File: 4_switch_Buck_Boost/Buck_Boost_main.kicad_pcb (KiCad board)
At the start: 4 copper layers, 98 parts, among them J1 Conn_02x02_Counter_Clockwise, J2 Screw_Terminal_2x5.08, J3 Screw_Terminal_2x2.54, J4 Screw_Terminal_2x5.08, M1 Fan, Q1 CSD18532Q5B, Q101 2N7002K, Q103 BSS83P, Q2 CSD18532Q5B, Q3 CSD18532Q5B, Q4 CSD18532Q5B, Q6 AO3400A, U1 LT8390EUFD_PBF

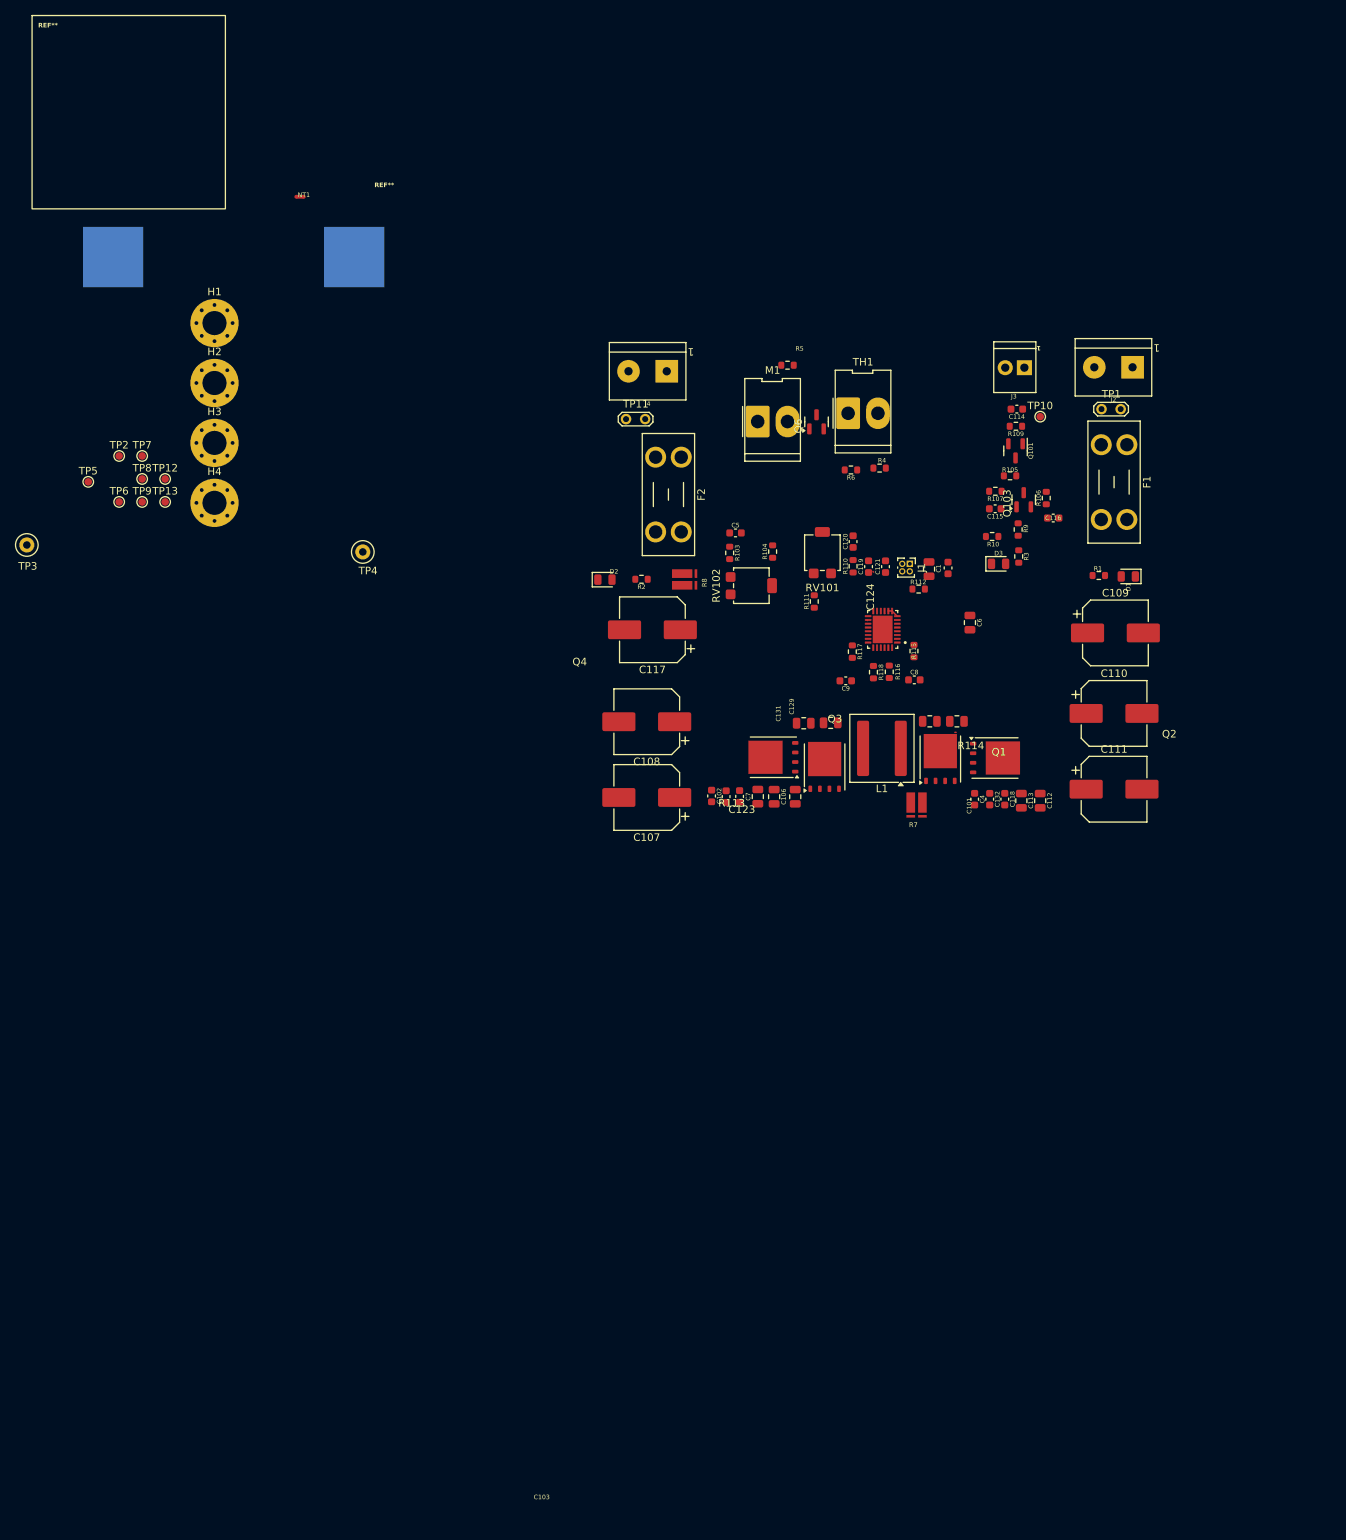
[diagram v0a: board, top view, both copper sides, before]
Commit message: improved Passive Components, Controller and Auxiliary Circuits
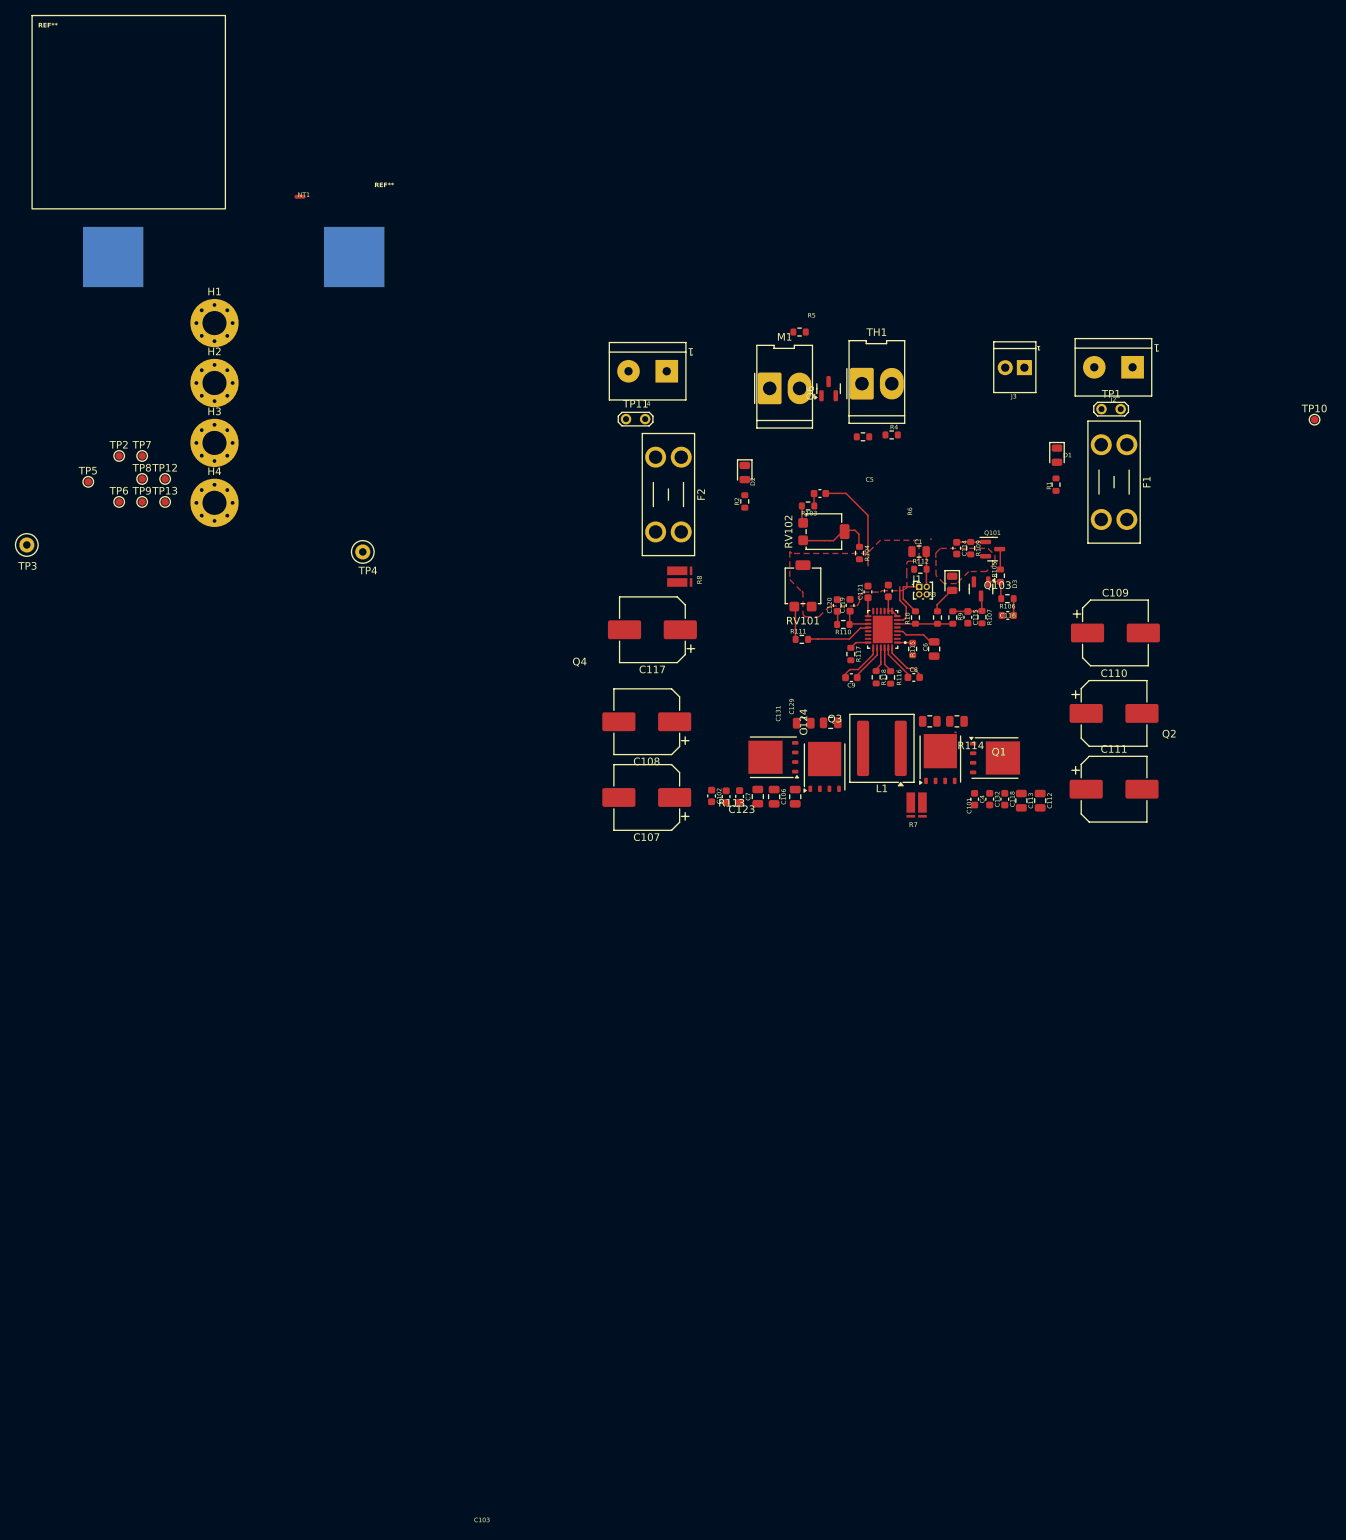
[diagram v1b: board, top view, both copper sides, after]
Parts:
- moved TP10 36.4 mm to (200.7, 73.0)
- moved D2 23.4 mm to (125.1, 80.0), turned to -90 degrees
- moved C114 20.1 mm to (153.2, 90.0), turned to -90 degrees
- moved D1 18.7 mm to (166.5, 77.7), turned to -90 degrees
- moved R109 17.3 mm to (155.1, 90.0), turned to -90 degrees
- moved R2 17.2 mm to (125.1, 83.8), turned to 90 degrees
- moved R107 16.8 mm to (156.6, 99.2), turned to -90 degrees
- moved C115 14.8 mm to (154.7, 99.2), turned to -90 degrees
- moved R10 14.8 mm to (147.8, 99.2), turned to 90 degrees
- moved R9 14.5 mm to (152.7, 99.2)
- moved R106 14.3 mm to (159.9, 96.7), turned to 180 degrees
- moved C116 14.3 mm to (160.0, 99.0), turned to 180 degrees
- moved R3 13.5 mm to (150.7, 99.2), turned to 90 degrees
- moved Q101 13.4 mm to (158.0, 90.2), turned to 0 degrees
- moved R1 13.3 mm to (166.4, 81.6), turned to 90 degrees
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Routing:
- net SYNC/SPRD: vias 0 -> 1
- net /INTVCC: vias 0 -> 1
- added copper zone on F.Cu, net GND
- added copper zone on F.Cu, net GNDA
- removed copper zone on In1.Cu, net GND

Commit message: Starting point for PCB Template Transformation
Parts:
- removed M1: Fan, Connector_Molex:Molex_KK-396_5273-02A_1x02_P3.96mm_Vertical
- removed Q6: AO3400A, Package_TO_SOT_SMD:SOT-23
- removed R4: 100K, rsx_resistors:R_0603_1608Metric
- removed R5: 10k, rsx_resistors:R_0603_1608Metric
- removed R6: 100, rsx_resistors:R_0603_1608Metric
- removed TH1: 10k, Connector_Molex:Molex_KK-396_5273-02A_1x02_P3.96mm_Vertical
- C6, C7: footprint rsx_capacitors:C_0805_2012Metric -> rsx_capacitors:C_0603_1608Metric
- L1: value 15u -> ~; footprint Inductor_SMD:L_Wuerth_WE-XHMI-8080 -> Inductor_SMD:L_Wuerth_WE-PD-Typ-LS
- R103: value 200k -> 10k
- R7: value 6m -> ~
- R8: value 15m -> ~
- RV102: value 50k -> 1M
- moved TP10 130.6 mm to (70.4, 63.7)
- moved D1 92.9 mm to (77.4, 51.5)
- moved R1 92.9 mm to (77.3, 55.4)
- moved R3 91.7 mm to (71.4, 53.1)
- moved D3 89.9 mm to (73.7, 51.7)
- moved HW2 72.5 mm to (49.7, 114.9)
- moved D2 64.1 mm to (67.5, 51.8)
- moved R2 64.1 mm to (67.5, 55.6)
- moved TP3 39.8 mm to (64.4, 69.8)
- moved F3 29.8 mm to (62.1, 80.8)
- moved C7 23.6 mm to (139.2, 102.9), turned to 0 degrees
- moved H4 20.5 mm to (54.1, 63.5)
- moved TP12 20.5 mm to (47.6, 60.3)
- moved TP2 20.5 mm to (41.5, 57.2)
- moved TP4 20.5 mm to (73.8, 70.0)
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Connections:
- R7 pad 2: SW1 -> Net-(L1-Pad1)
- R7 pad 3: Net-(L1-Pad1) -> SW1
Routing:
- net Net-(Q2-G): track 0.00 -> 1.08 mm, vias 0 -> 1
- net Net-(Q1-G): track 0.00 -> 1.07 mm, vias 0 -> 1
- net SYNC/SPRD: vias 1 -> 0
- net /INTVCC: vias 1 -> 0
- removed copper zone on F.Cu, net GND
- removed copper zone on F.Cu, net GNDA
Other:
- board text added: "Not ideal for Snubs, but they were always optional, will keep here but definitely sub-standard should be across DS of FET"

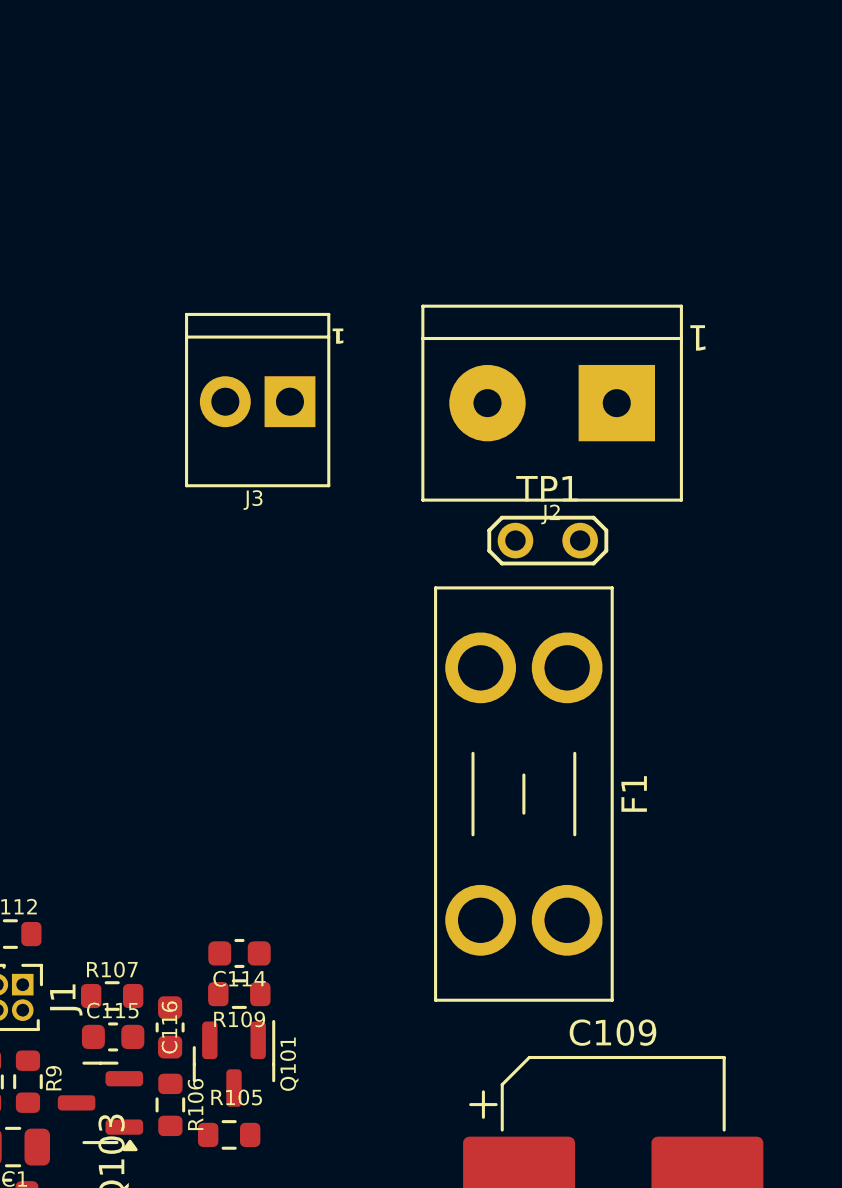
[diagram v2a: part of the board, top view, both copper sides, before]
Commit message: reverse polarity protection
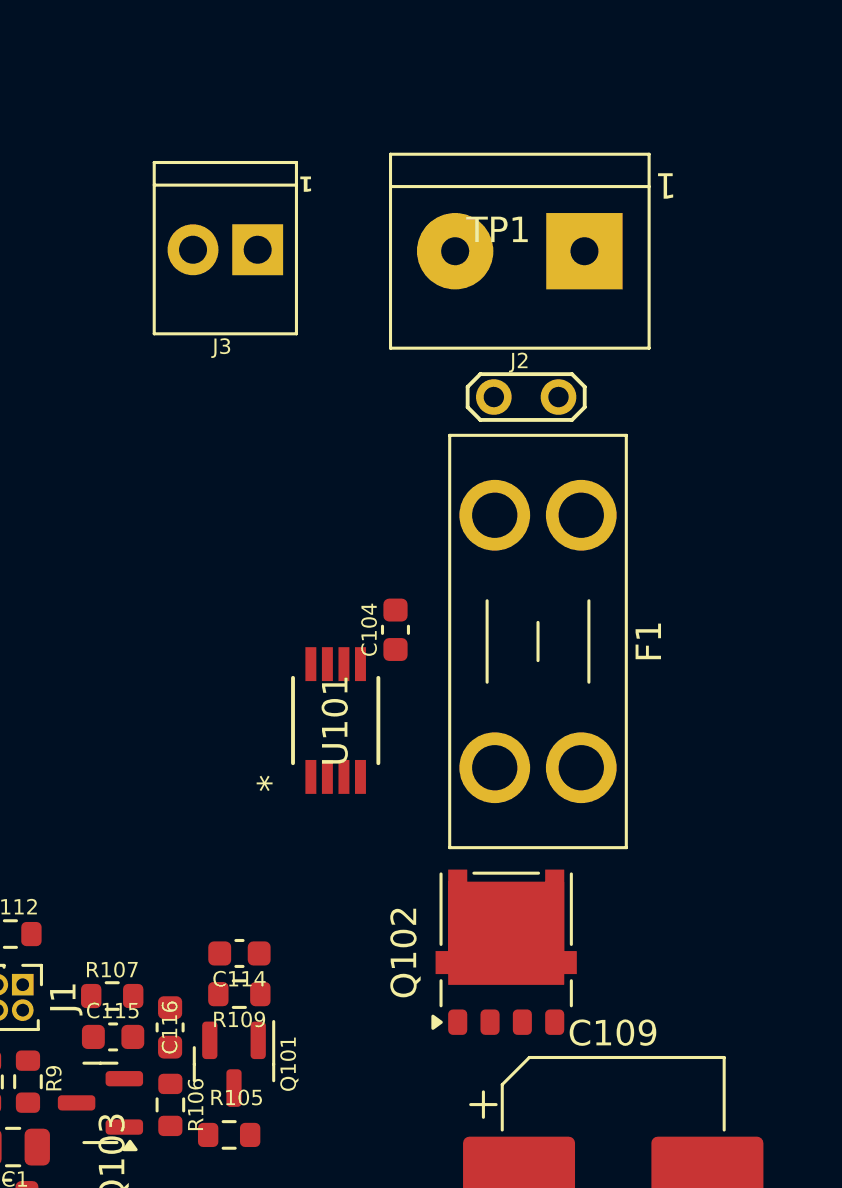
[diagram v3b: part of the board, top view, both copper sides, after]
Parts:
- added C104: 100n, rsx_capacitors:C_0603_1608Metric, F.Cu at (164.7, 81.6)
- added Q102: NVMFS6H836NLT1G, Package_SO:ONSemi_SO-8FL_488AA, F.Cu at (169.0, 94.2)
- added U101: LTC4372CMS8-PBF, LTC4372MS8:MS8_05-08-1660_ADI, F.Cu at (162.3, 85.1)
- moved J2 6.10 mm to (172.1, 66.7)
- moved J3 6.10 mm to (158.5, 66.6)
- moved F1 6.02 mm to (172.0, 77.1)
- moved TP1 5.70 mm to (168.5, 72.4)
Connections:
- F1 pad 2: Vin -> Net-(Q102-D)
